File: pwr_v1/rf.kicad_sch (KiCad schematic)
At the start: 1 part

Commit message: Schematic updated
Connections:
- net VCC renamed 3V3
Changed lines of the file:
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@@
 		)
 	)
-	(hierarchical_label "VCC"
+	(hierarchical_label "3V3"
 		(shape input)
 		(at 114.3 60.96 0)

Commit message: Schematic and layout updated; Motor driver alignments and planes;  Few components updated
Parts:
- J_RF1: footprint (none) -> Connector_PinHeader_2.54mm:PinHeader_2x04_P2.54mm_Vertical
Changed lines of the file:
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@@
 			)
 		)
-		(property "Footprint" ""
+		(property "Footprint" "Connector_PinHeader_2.54mm:PinHeader_2x04_P2.54mm_Vertical"
 			(at 100.33 63.5 0)
 			(effects
@@
 			)
 		)
-		(property "Description" "Generic connector, double row, 02x04, counter clockwise pin numbering scheme (similar to DIP package numbering), script generated (kicad-library-utils/schlib/autogen/connector/)"
+		(property "Description" ""
 			(at 100.33 63.5 0)
 			(effects

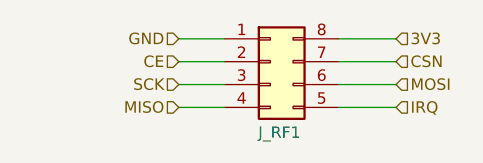
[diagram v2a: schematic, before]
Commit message: Schematic and layout updated; Layout placement and routing completed
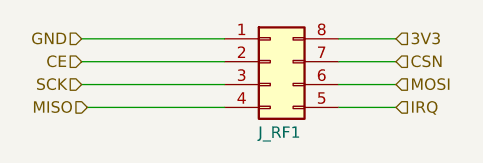
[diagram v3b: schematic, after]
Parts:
- J_RF1: footprint Connector_PinHeader_2.54mm:PinHeader_2x04_P2.54mm_Vertical -> Connector_PinSocket_2.54mm:PinSocket_2x04_P2.54mm_Vertical
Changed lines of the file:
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@@
 	(wire
 		(pts
-			(xy 90.17 60.96) (xy 95.25 60.96)
+			(xy 79.375 60.96) (xy 95.25 60.96)
 		)
 		(stroke
@@
 	(wire
 		(pts
-			(xy 90.17 68.58) (xy 95.25 68.58)
+			(xy 80.01 68.58) (xy 95.25 68.58)
+		)
+		(stroke
+			(width 0)
+			(type default)
+		)
+	)
+	(wire
+		(pts
+			(xy 79.375 63.5) (xy 95.25 63.5)
 		)
 		(stroke
@@
 	(wire
 		(pts
-			(xy 90.17 66.04) (xy 95.25 66.04)
-		)
-		(stroke
-			(width 0)
-			(type default)
-		)
-	)
-	(wire
-		(pts
-			(xy 90.17 63.5) (xy 95.25 63.5)
+			(xy 79.375 66.04) (xy 95.25 66.04)
 		)
 		(stroke
@@
 	(hierarchical_label "MISO"
 		(shape input)
-		(at 90.17 68.58 180)
+		(at 80.01 68.58 180)
 		(fields_autoplaced yes)
 		(effects
@@
 	(hierarchical_label "CE"
 		(shape input)
-		(at 90.17 63.5 180)
+		(at 79.375 63.5 180)
 		(fields_autoplaced yes)
 		(effects
@@
 	(hierarchical_label "SCK"
 		(shape input)
-		(at 90.17 66.04 180)
+		(at 79.375 66.04 180)
 		(fields_autoplaced yes)
 		(effects
@@
 	(hierarchical_label "GND"
 		(shape input)
-		(at 90.17 60.96 180)
+		(at 79.375 60.96 180)
 		(fields_autoplaced yes)
 		(effects
@@
 			)
 		)
-		(property "Footprint" "Connector_PinHeader_2.54mm:PinHeader_2x04_P2.54mm_Vertical"
+		(property "Footprint" "Connector_PinSocket_2.54mm:PinSocket_2x04_P2.54mm_Vertical"
 			(at 100.33 63.5 0)
 			(effects

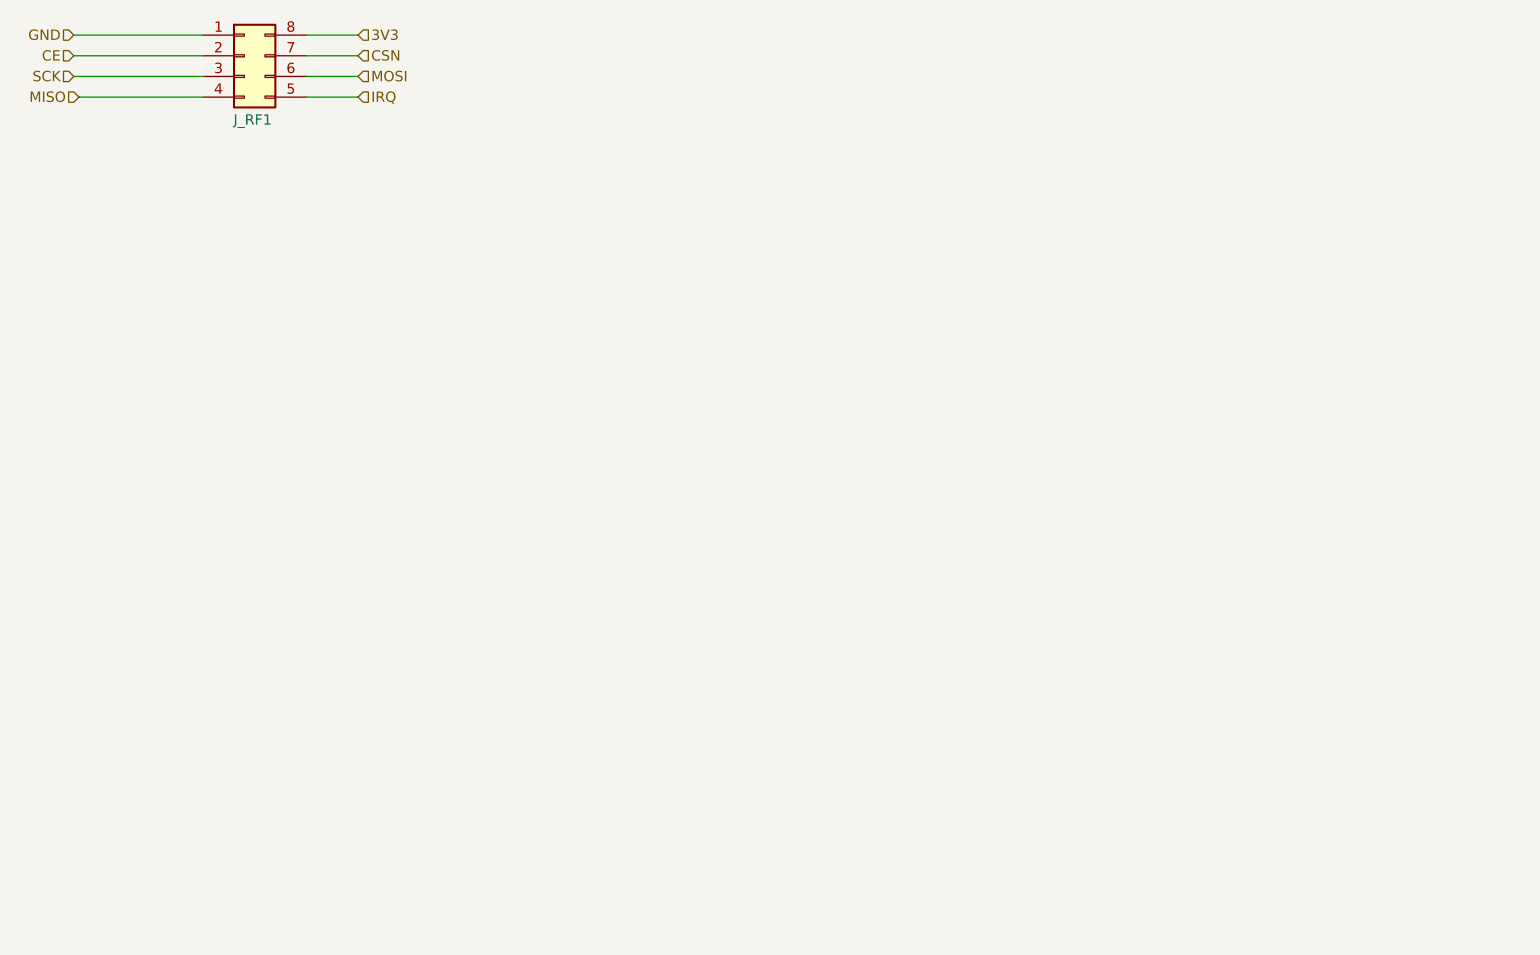
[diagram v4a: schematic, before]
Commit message: File structure enhanced.
Added uniform titleblocks and 3D renders for easier view, file cleanups.
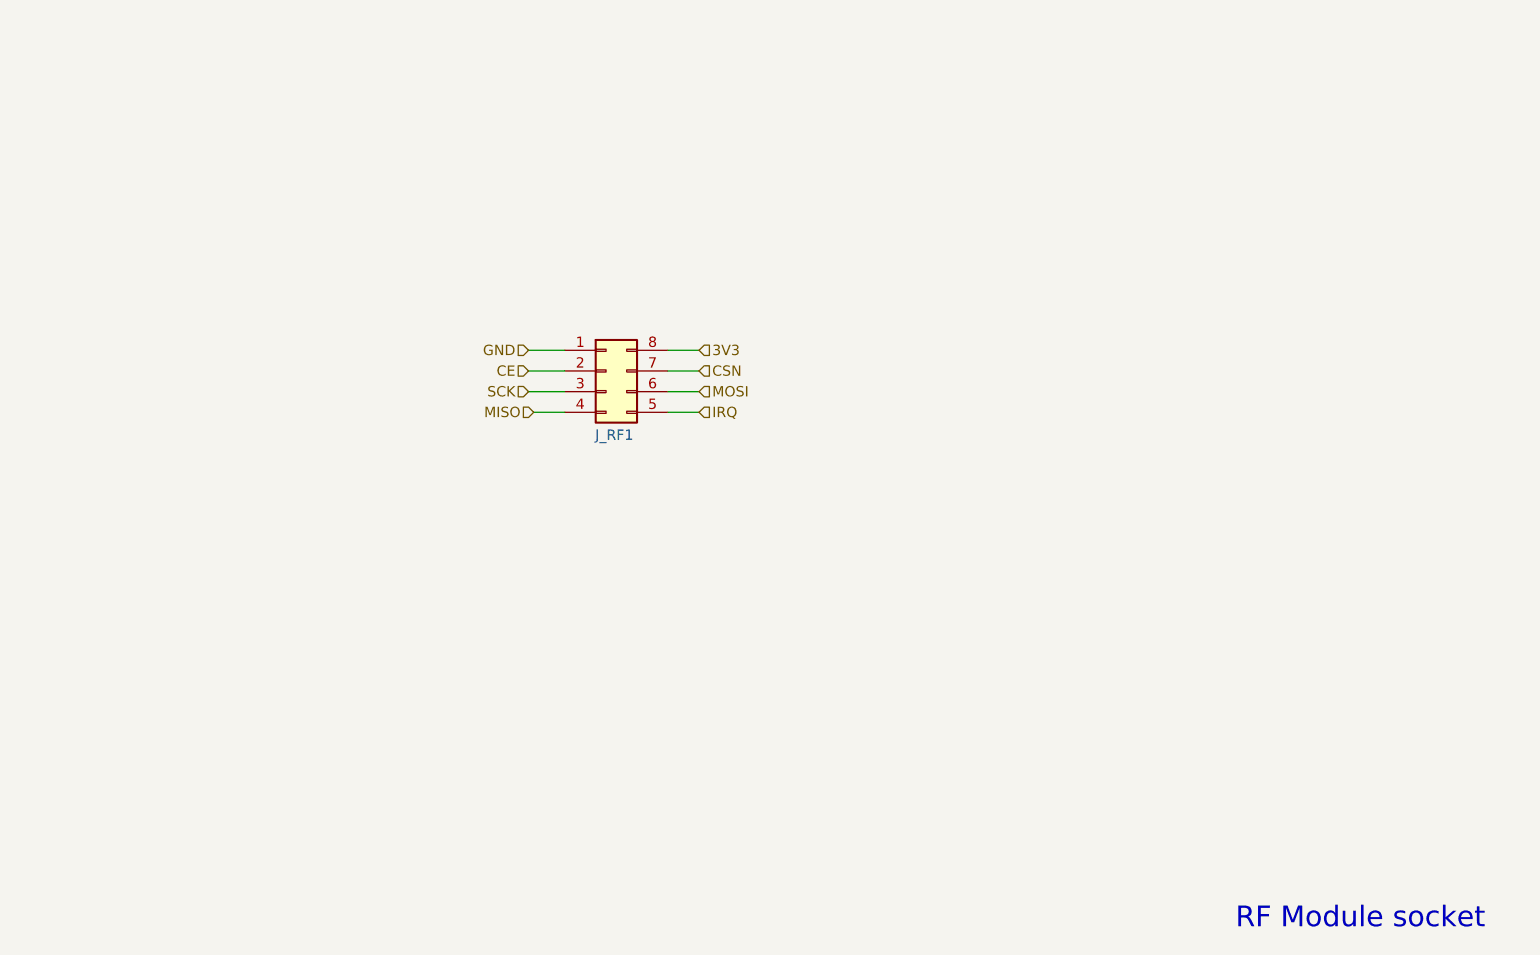
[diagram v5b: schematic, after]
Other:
- note added: "RF Module socket"
- title: (none) -> Power board
- moved on the sheet: J_RF1
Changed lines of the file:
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@@
 (kicad_sch
-	(version 20231120)
+	(version 20250114)
 	(generator "eeschema")
-	(generator_version "8.0")
-	(paper "A5")
-	(wire
-		(pts
-			(xy 107.95 68.58) (xy 114.3 68.58)
-		)
-		(stroke
-			(width 0)
-			(type default)
-		)
-	)
-	(wire
-		(pts
-			(xy 79.375 60.96) (xy 95.25 60.96)
-		)
-		(stroke
-			(width 0)
-			(type default)
-		)
-	)
-	(wire
-		(pts
-			(xy 107.95 66.04) (xy 114.3 66.04)
-		)
-		(stroke
-			(width 0)
-			(type default)
-		)
-	)
-	(wire
-		(pts
-			(xy 107.95 63.5) (xy 114.3 63.5)
-		)
-		(stroke
-			(width 0)
-			(type default)
-		)
-	)
-	(wire
-		(pts
-			(xy 80.01 68.58) (xy 95.25 68.58)
-		)
-		(stroke
-			(width 0)
-			(type default)
-		)
-	)
-	(wire
-		(pts
-			(xy 79.375 63.5) (xy 95.25 63.5)
-		)
-		(stroke
-			(width 0)
-			(type default)
-		)
-	)
-	(wire
-		(pts
-			(xy 107.95 60.96) (xy 114.3 60.96)
-		)
-		(stroke
-			(width 0)
-			(type default)
-		)
-	)
-	(wire
-		(pts
-			(xy 79.375 66.04) (xy 95.25 66.04)
+	(generator_version "9.0")
+	(paper "A4")
+	(title_block
+		(title "Power board")
+		(date "06-08-2024")
+		(rev "1")
+	)
+	(text "RF Module socket"
+		(exclude_from_sim no)
+		(at 237.49 169.545 0)
+		(effects
+			(font
+				(face "Gidole")
+				(size 2.54 2.54)
+			)
+		)
+	)
+	(wire
+		(pts
+			(xy 152.4 107.315) (xy 156.21 107.315)
+		)
+		(stroke
+			(width 0)
+			(type default)
+		)
+	)
+	(wire
+		(pts
+			(xy 135.255 99.695) (xy 139.7 99.695)
+		)
+		(stroke
+			(width 0)
+			(type default)
+		)
+	)
+	(wire
+		(pts
+			(xy 152.4 104.775) (xy 156.21 104.775)
+		)
+		(stroke
+			(width 0)
+			(type default)
+		)
+	)
+	(wire
+		(pts
+			(xy 152.4 102.235) (xy 156.21 102.235)
+		)
+		(stroke
+			(width 0)
+			(type default)
+		)
+	)
+	(wire
+		(pts
+			(xy 135.89 107.315) (xy 139.7 107.315)
+		)
+		(stroke
+			(width 0)
+			(type default)
+		)
+	)
+	(wire
+		(pts
+			(xy 135.255 102.235) (xy 139.7 102.235)
+		)
+		(stroke
+			(width 0)
+			(type default)
+		)
+	)
+	(wire
+		(pts
+			(xy 152.4 99.695) (xy 156.21 99.695)
+		)
+		(stroke
+			(width 0)
+			(type default)
+		)
+	)
+	(wire
+		(pts
+			(xy 135.255 104.775) (xy 139.7 104.775)
 		)
 		(stroke
@@
 	(hierarchical_label "MOSI"
 		(shape input)
-		(at 114.3 66.04 0)
-		(fields_autoplaced yes)
+		(at 156.21 104.775 0)
 		(effects
 			(font
@@
 	(hierarchical_label "MISO"
 		(shape input)
-		(at 80.01 68.58 180)
-		(fields_autoplaced yes)
+		(at 135.89 107.315 180)
 		(effects
 			(font
@@
 	(hierarchical_label "3V3"
 		(shape input)
-		(at 114.3 60.96 0)
-		(fields_autoplaced yes)
+		(at 156.21 99.695 0)
 		(effects
 			(font
@@
 	(hierarchical_label "CE"
 		(shape input)
-		(at 79.375 63.5 180)
-		(fields_autoplaced yes)
+		(at 135.255 102.235 180)
 		(effects
 			(font
@@
 	(hierarchical_label "SCK"
 		(shape input)
-		(at 79.375 66.04 180)
-		(fields_autoplaced yes)
+		(at 135.255 104.775 180)
 		(effects
 			(font
@@
 	(hierarchical_label "CSN"
 		(shape input)
-		(at 114.3 63.5 0)
-		(fields_autoplaced yes)
+		(at 156.21 102.235 0)
 		(effects
 			(font
@@
 	(hierarchical_label "IRQ"
 		(shape input)
-		(at 114.3 68.58 0)
-		(fields_autoplaced yes)
+		(at 156.21 107.315 0)
 		(effects
 			(font
@@
 	(hierarchical_label "GND"
 		(shape input)
-		(at 79.375 60.96 180)
-		(fields_autoplaced yes)
+		(at 135.255 99.695 180)
 		(effects
 			(font
@@
 	(symbol
 		(lib_id "Connector_Generic:Conn_02x04_Counter_Clockwise")
-		(at 100.33 63.5 0)
+		(at 144.78 102.235 0)
 		(unit 1)
 		(exclude_from_sim no)
@@
 		(dnp no)
 		(property "Reference" "J_RF1"
-			(at 101.346 71.374 0)
+			(at 145.796 110.109 0)
 			(effects
 				(font
@@
 		)
 		(property "Value" "Conn_02x04_Counter_Clockwise"
-			(at 101.6 57.15 0)
+			(at 146.05 95.885 0)
 			(effects
 				(font
@@
 		)
 		(property "Footprint" "Connector_PinSocket_2.54mm:PinSocket_2x04_P2.54mm_Vertical"
-			(at 100.33 63.5 0)
+			(at 144.78 102.235 0)
 			(effects
 				(font
@@
 		)
 		(property "Datasheet" "~"
-			(at 100.33 63.5 0)
+			(at 144.78 102.235 0)
 			(effects
 				(font
@@
 		)
 		(property "Description" "MFR.Part # 2.54-2*4 JLCPCB Part # C2977588"
-			(at 100.33 63.5 0)
-			(effects
-				(font
+			(at 144.78 102.235 0)
+			(effects
+				(font
